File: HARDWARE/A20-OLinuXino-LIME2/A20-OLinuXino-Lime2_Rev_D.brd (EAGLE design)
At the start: 84 x 59.6 mm, 428 parts, among them Q1 E4SB25.000F20E15(25MHz/20pF/2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, Q3 4SB24.000F20E15/5x3.2mm/20ppm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, Q4 32768Hz/6pF, T1 BC846B, U1 A20, U10 SY6280, U11 SY6280, U12 SY6280, U13 AXP209(QFN48), U14 MCP120T475I-TT, U15 SY8008C(AA)C, U16 SY7208(SOT23-6), U17 SY8008C(AA)C, U18 FIDUCIAL, U19 FIDUCIAL, U2 K4B4G1646D-BCK0, U20 FIDUCIAL, U21 FIDUCIAL, U3 K4B4G1646D-BCK0, U4 H27UBG8T2BTR, U5 RTL8211CL-GR, U6 AT24C16BN-SH, U7 NA(RCLAMP0524P), U8 NA(RCLAMP0524P), U9 NA(RCLAMP0524P)

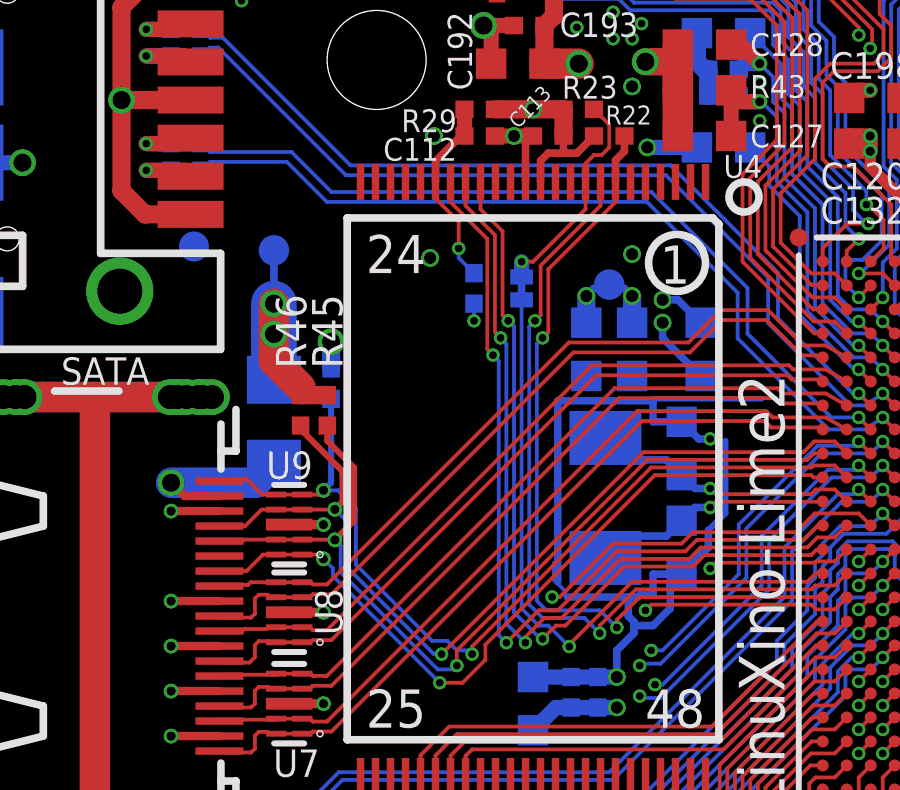
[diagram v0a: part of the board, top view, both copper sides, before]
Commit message: Re-route nand write-protect/PC16
Re-route the nand-write protect line to take up less board space in
critical area's. Some of the newly claimed area is not used yet.

Signed-off-by: Olliver Schinagl <o.schinagl@ultimaker.com>
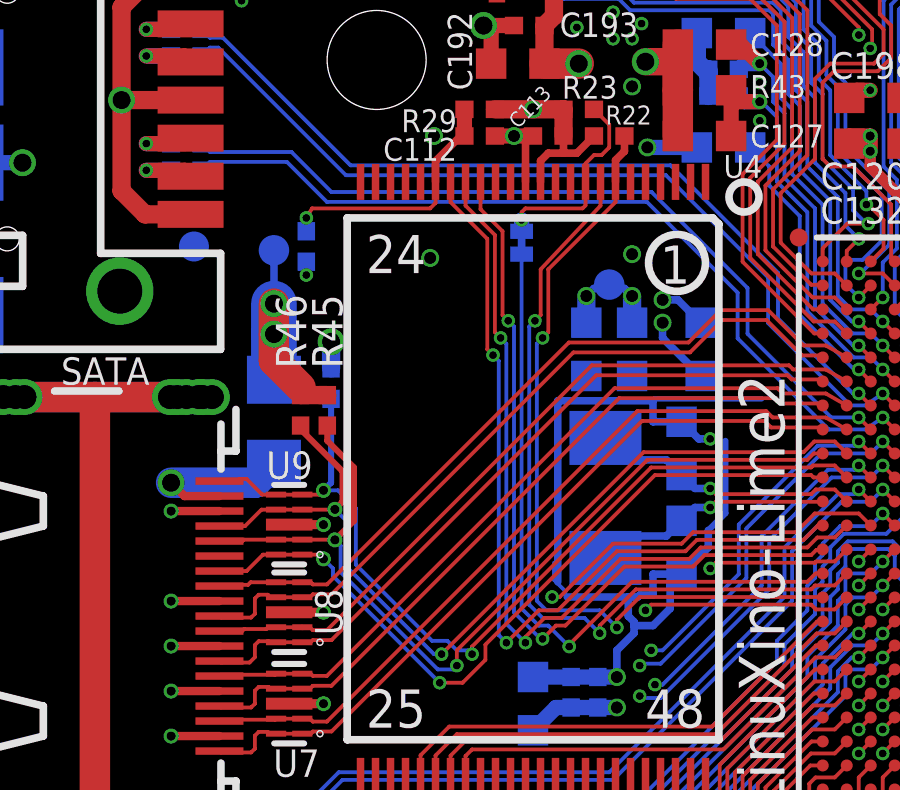
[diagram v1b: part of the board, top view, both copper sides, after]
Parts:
- moved R28 5.76 mm to (44.4, 80.9)
- moved NAND_E 1.52 mm to (51.6, 81.0)
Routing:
- net PC16/NWP: track 71.7 -> 67.3 mm
- net N$124: track 6.47 -> 8.60 mm
- net NCE0: track 21.9 -> 23.4 mm
- net N$232: track 7.38 -> 6.75 mm
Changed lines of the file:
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@@
 <element name="U20" library="SparkFunEagle-6-6-07" package="FIDUCIAL-1X3" value="FIDUCIAL" x="40.64" y="80.899" rot="MR0"/>
 <element name="U21" library="SparkFunEagle-6-6-07" package="FIDUCIAL-1X3" value="FIDUCIAL" x="113.284" y="45.974" rot="MR0"/>
-<element name="NAND_E" library="jumper" package="SJ_1_SMALLER_CLOSE_10MILS" value="Close" x="51.562" y="79.502" smashed="yes" rot="MR270">
-<attribute name="NAME" x="51.8795" y="78.74" size="1.016" layer="26" font="vector" ratio="20" rot="MR270"/>
-<attribute name="VALUE" x="53.467" y="81.407" size="1.27" layer="28" ratio="20" rot="MR270"/>
+<element name="NAND_E" library="jumper" package="SJ_1_SMALLER_CLOSE_10MILS" value="Close" x="51.562" y="81.026" smashed="yes" rot="MR270">
+<attribute name="NAME" x="51.8795" y="80.264" size="1.016" layer="26" font="vector" ratio="20" rot="MR270"/>
+<attribute name="VALUE" x="53.467" y="82.931" size="1.27" layer="28" ratio="20" rot="MR270"/>
 </element>
 <element name="5V_SATA_PWR" library="Penko" package="DW02R" value="CON2DW02R" x="36.195" y="98.298" smashed="yes" rot="R270">
@@
 <attribute name="VALUE" x="105.067" y="92.072" size="0.8128" layer="28" ratio="25" rot="MR0"/>
 </element>
-<element name="R28" library="rcl" package="R0402_TI" value="NA" x="49.9745" y="79.502" smashed="yes" rot="MR90">
-<attribute name="NAME" x="49.53" y="80.645" size="0.8128" layer="26" font="vector" ratio="20" rot="MR270"/>
-<attribute name="VALUE" x="48.5745" y="78.702" size="0.8128" layer="28" ratio="25" rot="MR90"/>
+<element name="R28" library="rcl" package="R0402_TI" value="NA" x="44.3865" y="80.899" smashed="yes" rot="MR90">
+<attribute name="NAME" x="43.942" y="82.042" size="0.8128" layer="26" font="vector" ratio="20" rot="MR270"/>
+<attribute name="VALUE" x="42.9865" y="80.099" size="0.8128" layer="28" ratio="25" rot="MR90"/>
 </element>
 <element name="LAN" library="OLIMEX_CONNECTORS" package="TM211Q01FM22_SH" value="TM211Q01FM22_SH" x="108.712" y="55.372" smashed="yes" rot="R270">
@@
 <wire x1="52.451" y1="68.2625" x2="52.1335" y2="68.2625" width="0.127" layer="16"/>
 <wire x1="52.1335" y1="68.2625" x2="51.562" y2="68.834" width="0.127" layer="16"/>
-<wire x1="51.562" y1="68.834" x2="51.562" y2="79.121" width="0.127" layer="16"/>
+<wire x1="51.562" y1="68.834" x2="51.562" y2="80.645" width="0.127" layer="16"/>
 <via x="53.1495" y="67.564" extent="1-16" drill="0.254"/>
 </signal>
@@
 <wire x1="61.345" y1="69.6" x2="62" y2="69.6" width="0.127" layer="1"/>
 <wire x1="52.0065" y1="78.4225" x2="52.197" y2="78.613" width="0.127" layer="1"/>
-<wire x1="52.197" y1="78.613" x2="52.197" y2="80.264" width="0.127" layer="1"/>
-<wire x1="52.197" y1="80.264" x2="54.193" y2="82.26" width="0.127" layer="1"/>
+<wire x1="52.197" y1="78.613" x2="52.197" y2="80.137" width="0.127" layer="1"/>
+<wire x1="52.197" y1="80.137" x2="54.193" y2="82.26" width="0.127" layer="1"/>
 <wire x1="54.193" y1="82.26" x2="54.193" y2="83.052" width="0.127" layer="1"/>
 <wire x1="54.1655" y1="68.0085" x2="54.1655" y2="68.2625" width="0.127" layer="1"/>
@@
 <wire x1="48.693" y1="83.745" x2="49.53" y2="84.582" width="0.254" layer="1"/>
 <wire x1="49.53" y1="84.582" x2="49.657" y2="84.582" width="0.254" layer="1"/>
-<wire x1="49.9745" y1="80.01" x2="49.4665" y2="80.518" width="0.127" layer="16"/>
-<wire x1="49.4665" y1="80.518" x2="49.4665" y2="80.8355" width="0.127" layer="16"/>
-<wire x1="49.4665" y1="80.8355" x2="49.4665" y2="81.7245" width="0.127" layer="1"/>
-<wire x1="48.693" y1="82.498" x2="48.693" y2="83.052" width="0.127" layer="1"/>
-<wire x1="49.4665" y1="81.7245" x2="48.693" y2="82.498" width="0.127" layer="1"/>
-<via x="49.4665" y="80.8355" extent="1-16" drill="0.254"/>
+<wire x1="44.3865" y1="81.407" x2="44.3865" y2="81.8515" width="0.127" layer="16"/>
+<wire x1="48.693" y1="82.348" x2="48.693" y2="83.052" width="0.127" layer="1"/>
+<wire x1="44.3865" y1="81.8515" x2="44.577" y2="82.169" width="0.127" layer="1"/>
+<wire x1="44.577" y1="82.169" x2="48.514" y2="82.169" width="0.127" layer="1"/>
+<wire x1="48.514" y1="82.169" x2="48.693" y2="82.348" width="0.127" layer="1"/>
+<via x="44.3865" y="81.8515" extent="1-16" drill="0.254"/>
 </signal>
 <signal name="PB3">
@@
 <wire x1="54.483" y1="84.201" x2="54.483" y2="84.963" width="0.127" layer="1"/>
 <wire x1="54.483" y1="84.963" x2="53.975" y2="85.471" width="0.127" layer="1"/>
-<wire x1="51.562" y1="80.391" x2="51.943" y2="80.391" width="0.127" layer="1"/>
-<wire x1="51.943" y1="80.391" x2="53.693" y2="82.141" width="0.127" layer="1"/>
-<wire x1="53.693" y1="82.141" x2="53.693" y2="83.052" width="0.127" layer="1"/>
-<wire x1="51.562" y1="79.883" x2="51.562" y2="80.391" width="0.508" layer="16"/>
-<via x="51.562" y="80.391" extent="1-16" drill="0.254"/>
+<wire x1="51.943" y1="80.391" x2="51.562" y2="81.788" width="0" layer="19" extent="1-16"/>
+<wire x1="51.562" y1="81.788" x2="51.562" y2="82.042" width="0.127" layer="1"/>
+<wire x1="51.562" y1="82.042" x2="51.689" y2="82.169" width="0.127" layer="1"/>
+<wire x1="51.689" y1="82.169" x2="53.594" y2="82.169" width="0.127" layer="1"/>
+<wire x1="53.594" y1="82.169" x2="53.693" y2="82.268" width="0.127" layer="1"/>
+<wire x1="53.693" y1="82.268" x2="53.693" y2="83.052" width="0.127" layer="1"/>
+<wire x1="51.562" y1="81.407" x2="51.562" y2="81.788" width="0.508" layer="16"/>
+<via x="51.562" y="81.788" extent="1-16" drill="0.254"/>
 </signal>
 <signal name="PC19">
@@
 <wire x1="54.61" y1="70.993" x2="56.896" y2="70.993" width="0.127" layer="1"/>
 <wire x1="43.307" y1="100.838" x2="44.577" y2="100.838" width="0.508" layer="1"/>
-<wire x1="52.578" y1="69.215" x2="55.499" y2="69.215" width="0.127" layer="14"/>
-<wire x1="55.499" y1="69.215" x2="59.944" y2="73.66" width="0.127" layer="14"/>
-<wire x1="59.944" y1="73.66" x2="59.944" y2="87.249" width="0.127" layer="14"/>
-<wire x1="59.944" y1="87.249" x2="59.69" y2="87.503" width="0.127" layer="14"/>
-<wire x1="59.69" y1="87.503" x2="57.785" y2="87.503" width="0.127" layer="14"/>
-<wire x1="57.785" y1="87.503" x2="55.118" y2="90.17" width="0.127" layer="14"/>
-<wire x1="55.118" y1="90.17" x2="53.848" y2="90.17" width="0.127" layer="14"/>
-<wire x1="53.848" y1="90.17" x2="51.943" y2="92.075" width="0.127" layer="14"/>
-<wire x1="51.943" y1="92.075" x2="50.292" y2="92.075" width="0.127" layer="14"/>
-<wire x1="50.292" y1="92.075" x2="49.149" y2="93.218" width="0.127" layer="14"/>
-<wire x1="49.149" y1="93.218" x2="49.149" y2="93.98" width="0.127" layer="14"/>
-<wire x1="49.149" y1="93.98" x2="48.895" y2="94.234" width="0.127" layer="14"/>
-<wire x1="48.895" y1="94.234" x2="48.895" y2="96.901" width="0.127" layer="14"/>
-<wire x1="48.895" y1="96.901" x2="47.879" y2="97.917" width="0.127" layer="14"/>
-<wire x1="47.879" y1="97.917" x2="47.879" y2="98.425" width="0.127" layer="14"/>
-<wire x1="47.879" y1="98.425" x2="47.498" y2="98.806" width="0.127" layer="14"/>
-<wire x1="47.498" y1="98.806" x2="45.339" y2="98.806" width="0.127" layer="14"/>
-<wire x1="45.339" y1="98.806" x2="43.307" y2="100.838" width="0.127" layer="14"/>
-<wire x1="52.578" y1="69.215" x2="52.578" y2="73.025" width="0.127" layer="14"/>
-<wire x1="52.578" y1="73.025" x2="49.657" y2="75.946" width="0.127" layer="14"/>
-<wire x1="49.657" y1="75.946" x2="49.657" y2="78.105" width="0.127" layer="14"/>
-<wire x1="49.657" y1="78.105" x2="49.9745" y2="78.4225" width="0.127" layer="14"/>
-<wire x1="49.9745" y1="78.4225" x2="49.9745" y2="78.994" width="0.127" layer="16"/>
+<wire x1="52.578" y1="69.215" x2="46.482" y2="69.215" width="0.127" layer="14"/>
+<wire x1="46.482" y1="69.215" x2="46.2915" y2="69.4055" width="0.127" layer="14"/>
+<wire x1="46.2915" y1="69.4055" x2="46.2915" y2="78.0415" width="0.127" layer="14"/>
+<wire x1="46.2915" y1="78.0415" x2="44.3865" y2="79.3115" width="0.127" layer="14"/>
+<wire x1="44.3865" y1="79.3115" x2="44.3865" y2="79.9465" width="0.127" layer="14"/>
+<wire x1="44.3865" y1="79.9465" x2="44.3865" y2="80.391" width="0.127" layer="16"/>
 <via x="52.578" y="69.215" extent="1-16" drill="0.254"/>
 <via x="43.307" y="100.838" extent="1-16" drill="0.254"/>
-<via x="49.9745" y="78.4225" extent="1-16" drill="0.254"/>
+<via x="44.3865" y="79.9465" extent="1-16" drill="0.254"/>
+<wire x1="43.307" y1="100.838" x2="41.656" y2="100.838" width="0.127" layer="14"/>
+<wire x1="41.656" y1="100.838" x2="40.005" y2="99.187" width="0.127" layer="14"/>
+<wire x1="40.005" y1="99.187" x2="40.005" y2="91.694" width="0.127" layer="14"/>
+<wire x1="40.005" y1="91.694" x2="36.322" y2="88.011" width="0.127" layer="14"/>
+<wire x1="36.322" y1="88.011" x2="36.322" y2="78.74" width="0.127" layer="14"/>
+<wire x1="36.322" y1="78.74" x2="37.719" y2="77.343" width="0.127" layer="14"/>
+<wire x1="37.719" y1="77.343" x2="39.751" y2="77.343" width="0.127" layer="14"/>
+<wire x1="39.751" y1="77.343" x2="42.3545" y2="79.9465" width="0.127" layer="14"/>
+<wire x1="42.3545" y1="79.9465" x2="44.3865" y2="79.9465" width="0.127" layer="14"/>
 </signal>
 <signal name="PB13">

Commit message: Rename R28 to NAND_WP
R28 is a spot where a zero ohm resistor can be placed to control the
NAND flash's Write Protect. This commit renames this resistor to NAND_WP
and marks it as such on the silk-screen.

Signed-off-by: Olliver Schinagl <o.schinagl@ultimaker.com>
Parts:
- renumbered R28 to NAND_WP
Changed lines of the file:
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@@
 <text x="106.045" y="71.755" size="1.016" layer="26" font="vector" ratio="20" rot="MR0">+</text>
 <text x="51.181" y="56.134" size="1.016" layer="25" font="vector" ratio="20">+</text>
+<wire x1="44.831" y1="80.137" x2="44.6405" y2="79.9465" width="0.127" layer="22" curve="-90"/>
+<wire x1="44.6405" y1="79.9465" x2="44.1325" y2="79.9465" width="0.127" layer="22"/>
+<wire x1="44.1325" y1="79.9465" x2="43.942" y2="80.137" width="0.127" layer="22" curve="-90"/>
+<wire x1="43.942" y1="80.137" x2="43.942" y2="81.661" width="0.127" layer="22"/>
+<wire x1="43.942" y1="81.661" x2="44.1325" y2="81.8515" width="0.127" layer="22" curve="-90"/>
+<wire x1="44.1325" y1="81.8515" x2="44.6405" y2="81.8515" width="0.127" layer="22"/>
+<wire x1="44.6405" y1="81.8515" x2="44.831" y2="81.661" width="0.127" layer="22" curve="-90"/>
+<wire x1="44.831" y1="81.661" x2="44.831" y2="80.137" width="0.127" layer="22"/>
 </plain>
 <attributes>
@@
 </element>
 <element name="+5V" library="gogo" package="TESTPAD_40-ROUND" value="TESTPADTESTPAD_40-ROUND" x="43.307" y="80.772" smashed="yes" rot="MR0">
-<attribute name="NAME" x="44.577" y="81.534" size="1.016" layer="26" font="vector" ratio="20" rot="MR0"/>
+<attribute name="NAME" x="41.7195" y="79.3115" size="1.016" layer="26" font="vector" ratio="20" rot="MR90"/>
 </element>
 <element name="BAT" library="gogo" package="TESTPAD_40-ROUND" value="TESTPADTESTPAD_40-ROUND" x="102.362" y="85.471" smashed="yes" rot="MR0">
@@
 <attribute name="VALUE" x="105.067" y="92.072" size="0.8128" layer="28" ratio="25" rot="MR0"/>
 </element>
-<element name="R28" library="rcl" package="R0402_TI" value="NA" x="44.3865" y="80.899" smashed="yes" rot="MR90">
-<attribute name="NAME" x="43.942" y="82.042" size="0.8128" layer="26" font="vector" ratio="20" rot="MR270"/>
+<element name="NAND_WP" library="rcl" package="R0402_TI" value="NA" x="44.3865" y="80.899" smashed="yes" rot="MR90">
+<attribute name="NAME" x="45.212" y="78.486" size="0.8128" layer="26" font="vector" ratio="20" rot="MR90"/>
 <attribute name="VALUE" x="42.9865" y="80.099" size="0.8128" layer="28" ratio="25" rot="MR90"/>
 </element>
@@
 <contactref element="C112" pad="2"/>
 <contactref element="U4" pad="19"/>
-<contactref element="R28" pad="2"/>
+<contactref element="NAND_WP" pad="2"/>
 <wire x1="49.657" y1="84.582" x2="49.657" y2="85.471" width="0.508" layer="1"/>
 <wire x1="48.693" y1="83.052" x2="48.693" y2="83.745" width="0.254" layer="1"/>
@@
 <contactref element="U1" pad="M21"/>
 <contactref element="GPIO-4" pad="18"/>
-<contactref element="R28" pad="1"/>
+<contactref element="NAND_WP" pad="1"/>
 <wire x1="62.8" y1="72" x2="63.2" y2="71.6" width="0.127" layer="1"/>
 <wire x1="60.706" y1="71.374" x2="61.332" y2="72" width="0.127" layer="1"/>
